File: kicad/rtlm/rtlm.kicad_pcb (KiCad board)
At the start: 6 copper layers, 200 x 110 mm, 265 parts, among them IC1 ESP32-S3FN8, IC2 TPS25940ARVCR, IC3 PE4259, IC4 TPS2553DBVR, IC5 TLV9004IDR, IC6 TLV9004IDR, IC7 TCAN1042HGVDR, IC8 TPS2553DBVR, IC9 TLC59116IPWR, J1 USB_C_Receptacle_USB2.0_16P, J10 TEMP_2, J11 TEMP_3, J12 TEMP_4, J13 ANALOG_1, J14 ANALOG_2, J15 ANALOG_3, J16 ANALOG_4, J17 DM3AT-SF-PEJM5, J18 CAN_EXPANSION, J19 BATTERY_VOLTAGE_SENSE_LINE, J2 Conn_01x02, J3 UART_DEBUG_3V3, J4 LORA_ANT, J5 PULSE_1, J6 PULSE_2, J7 PULSE_3, J8 PULSE_4, J9 TEMP_1, Q1 DMP2035U-7, SW1 SW_Push, SW2 SW_Push, U1 TPS62130A, U10 RV-3028-C7, U2 TPS2116DRL, U3 TPD2EUSB30, U4 SX1262IMLTRT, U5 SN74LVC14ADR, U6 MCP3208-BI/SL, U7 REF3025AIDBZR, U8 AMC3330, U9 ADS1115IDGS, Y1 40MHz, Y2 TG2520SMN 32.0000M-MCGNNM3

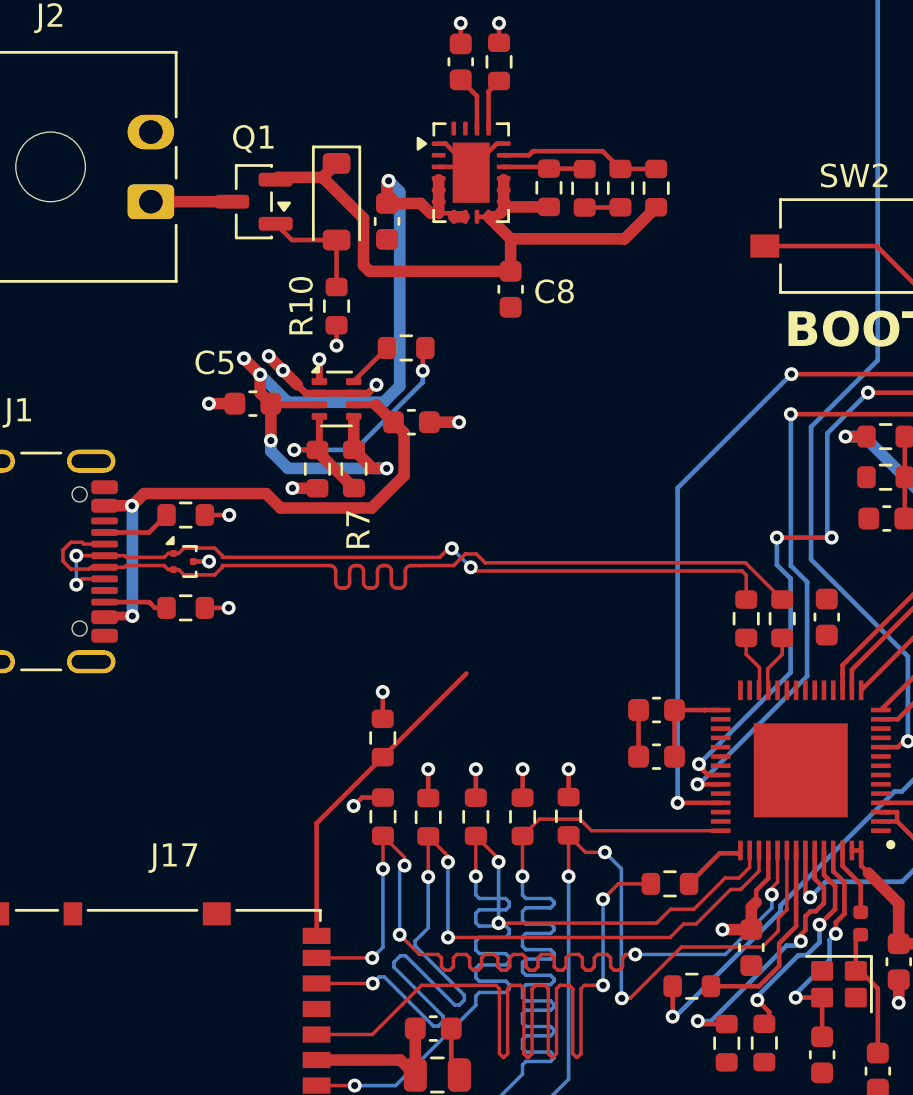
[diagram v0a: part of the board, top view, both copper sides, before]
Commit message: feat: widen power traces, add thermal vias
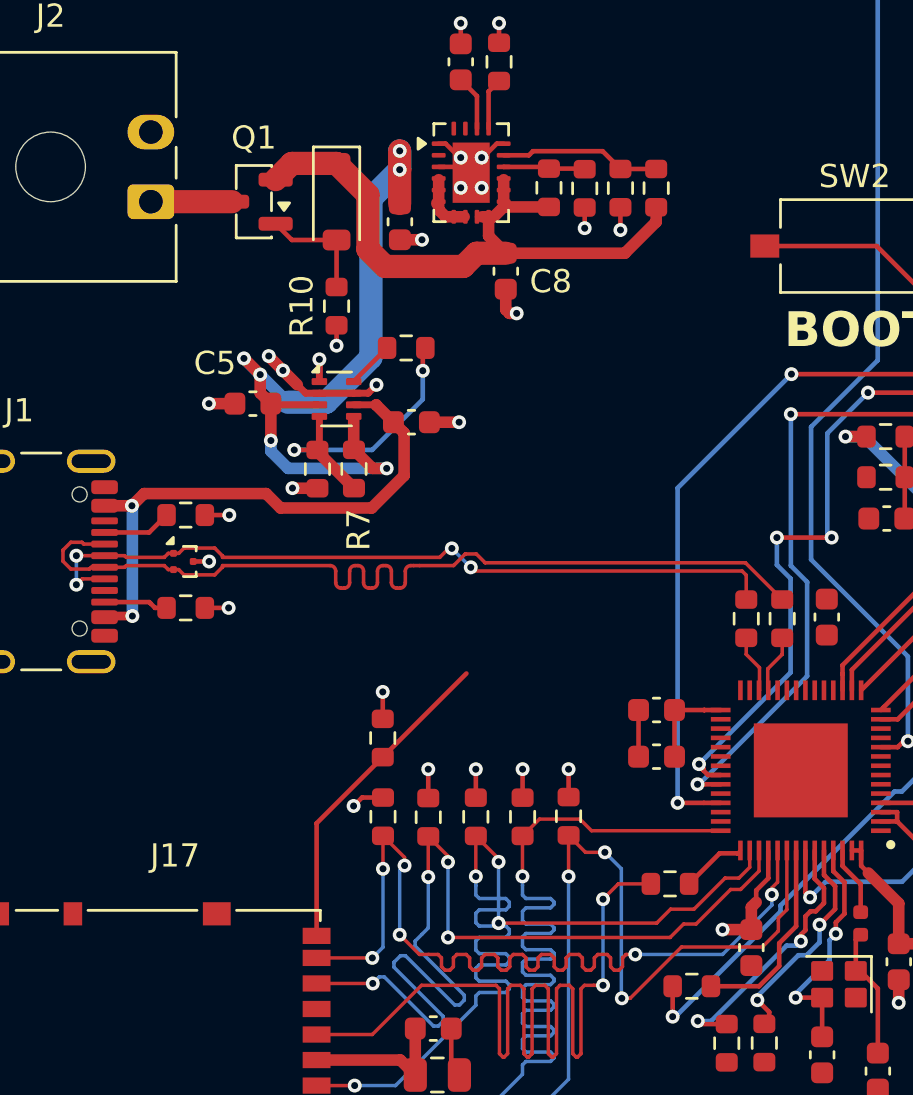
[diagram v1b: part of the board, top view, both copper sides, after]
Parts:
- moved C8 0.81 mm to (219.3, 197.5)
- moved C9 0.56 mm to (214.7, 195.4)
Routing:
- net GND: track 118.3 -> 121.0 mm, vias 16 -> 24
- net /EXT_5V_PROTECTED: track 38.0 -> 36.6 mm, vias 5 -> 6

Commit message: feat: move buck and wire up
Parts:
- moved C2 38.6 mm to (228.2, 187.5)
- moved C4 38.6 mm to (228.2, 185.8)
- moved C1 38.6 mm to (232.1, 191.2)
- moved L1 38.6 mm to (236.8, 187.8)
- moved R6 38.6 mm to (230.9, 183.8)
- moved C3 38.6 mm to (236.5, 191.8)
- moved R5 38.6 mm to (234.0, 183.8)
- moved U1 38.6 mm to (232.1, 187.6)
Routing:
- net +3.3V: track 89.7 -> 134.5 mm, vias 10 -> 12
- net GND: track 121.0 -> 136.7 mm, vias 24 -> 32
- net /5V_SYS: track 19.1 -> 28.9 mm, vias 5 -> 7
- net Net-(L1-Pad1): track 6.46 -> 4.58 mm

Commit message: feat: power wiring around IC1
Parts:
- added C80: 10uF, Capacitor_SMD:C_0805_2012Metric, F.Cu at (242.5, 224.6)
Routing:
- net GND: track 136.7 -> 142.9 mm, vias 32 -> 47
- net +3.3V: track 134.5 -> 140.6 mm, vias 12 -> 16
- net Net-(IC1-VDD3P3_1): track 5.51 -> 10.2 mm
- net /I2C_SDA: track 177.2 -> 176.6 mm

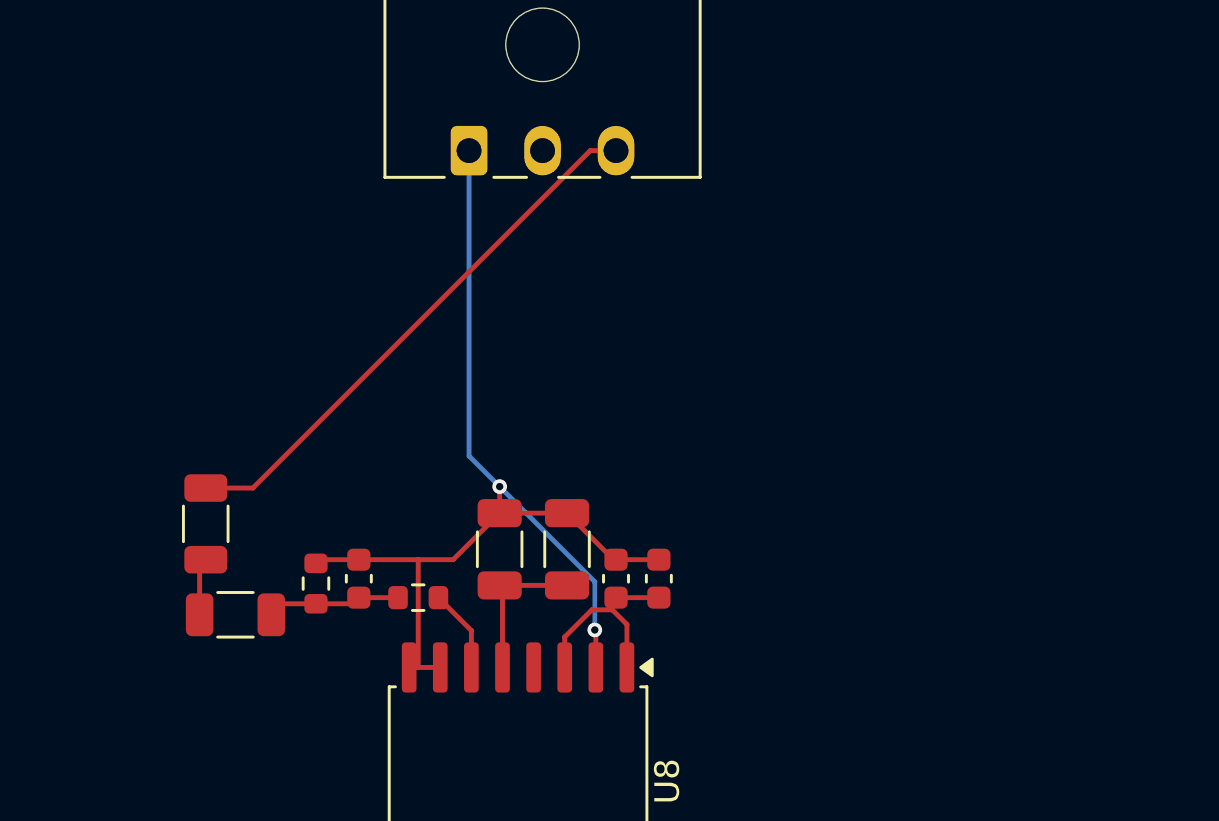
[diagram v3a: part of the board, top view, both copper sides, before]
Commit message: feat: add voltage sense fuse and route sense upper half
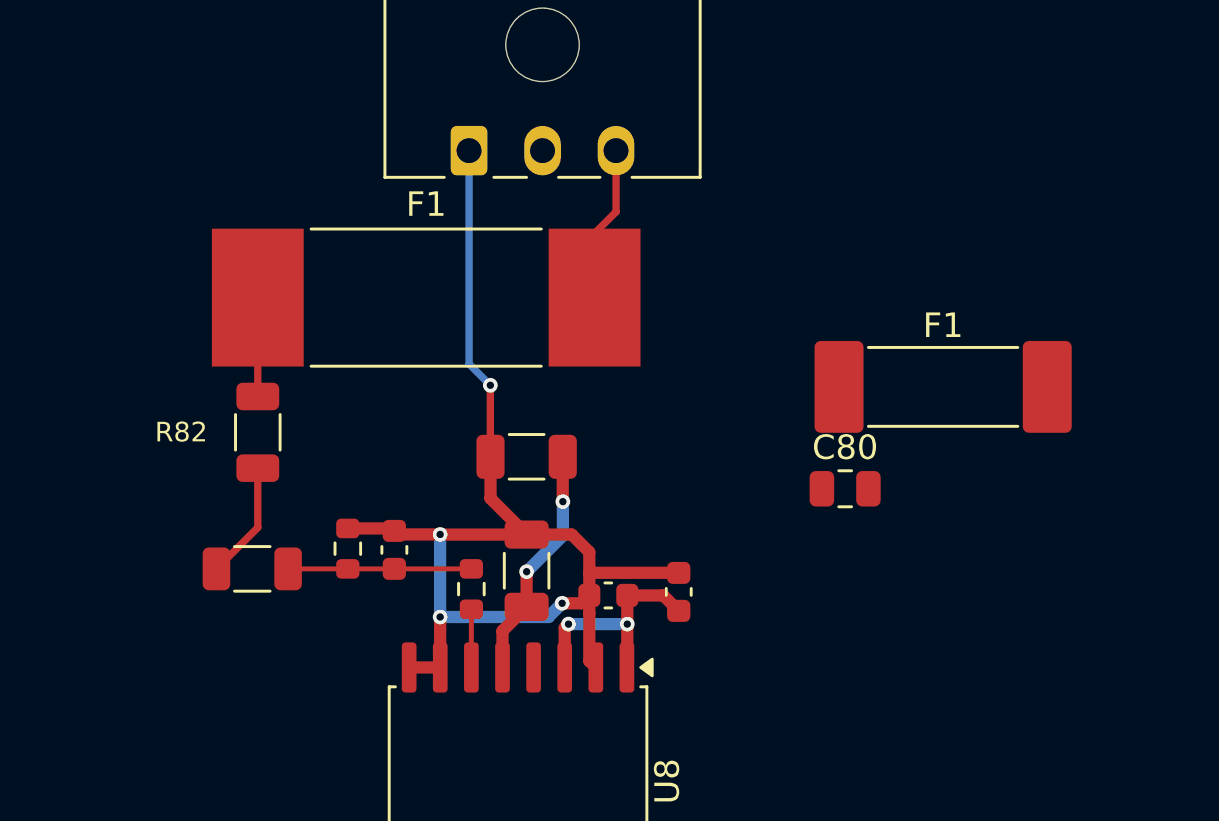
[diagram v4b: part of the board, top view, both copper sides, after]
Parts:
- added C80: 10uF, Capacitor_SMD:C_0805_2012Metric, F.Cu at (363.6, 188.3)
- added F1: 160mA T 250VDC, Fuse:Fuse_Schurter_UMT250, F.Cu at (367.6, 184.1)
- added F1: 160mA T 250VDC, rtlm_local:Fuse_Schurter_UMT-H_160mA, F.Cu at (346.5, 180.5)
- moved R82 4.30 mm to (339.6, 186.0)
- moved C71 4.12 mm to (350.6, 187.0), turned to 0 degrees
- moved C69 2.62 mm to (356.8, 192.5)
- moved R90 2.20 mm to (348.3, 192.4), turned to -90 degrees
- moved C70 2.18 mm to (353.9, 192.7), turned to 0 degrees
- moved R83 2.00 mm to (339.4, 191.6)
- moved R84 1.93 mm to (343.3, 190.8)
- moved C74 1.87 mm to (345.2, 190.8)
- moved C72 1.41 mm to (350.6, 191.7)
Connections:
- R82 pad 1: /PACK_POS -> /PACK_POS_FUSED
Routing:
- net /PACK_POS: track 22.5 -> 6.36 mm
- net /PACK_POS_FUSED: track 0.00 -> 4.04 mm
- net /HLDO_OUT: track 6.08 -> 9.62 mm, vias 0 -> 2
- net /PACK_NEG: track 45.6 -> 48.5 mm, vias 2 -> 4
- net Net-(R82-Pad2): track 2.35 -> 4.81 mm
- net Net-(C74-Pad1): track 5.46 -> 7.48 mm
- net /PACK_V_SENSE: track 3.41 -> 2.38 mm
- net /VMON_ISO_SUPPLY: track 8.56 -> 9.54 mm, vias 0 -> 2
